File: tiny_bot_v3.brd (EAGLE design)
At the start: 49.7 x 81.5 mm, 31 parts, among them IC1 SN754410PDIP, U1 ATMEGA328P_PDIP, X1 16 MHz

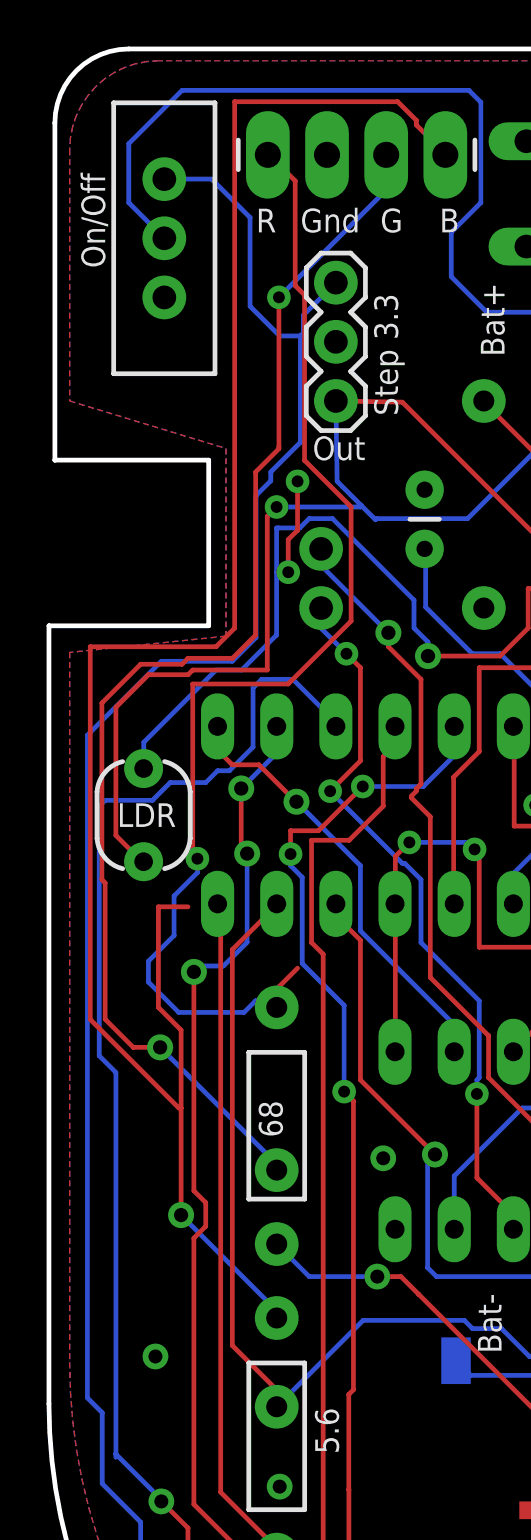
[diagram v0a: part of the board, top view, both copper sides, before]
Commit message: Fixed clearance error and added gerber files
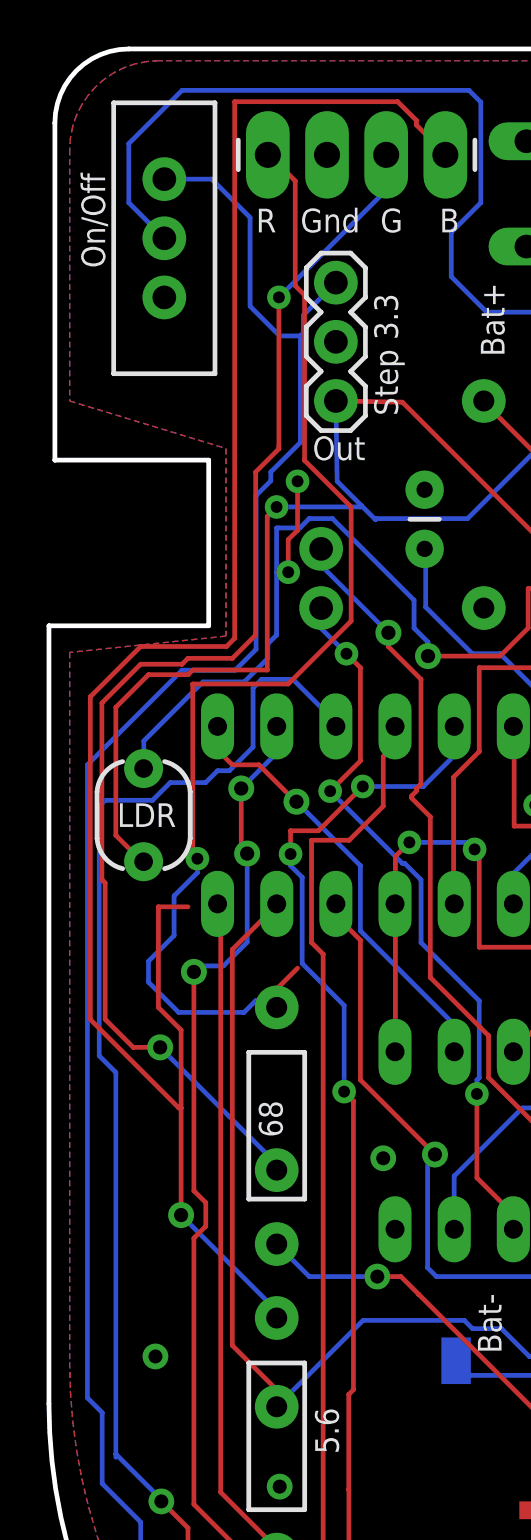
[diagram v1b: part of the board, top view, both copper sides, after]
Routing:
- net N$6: track 81.8 -> 80.7 mm
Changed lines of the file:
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@@
 <wire x1="16.4" y1="54.2" x2="19.5" y2="54.2" width="0.2032" layer="1"/>
 <wire x1="16.4" y1="54.7" x2="16.4" y2="54.2" width="0.2032" layer="16"/>
-<wire x1="4.2" y1="50.5" x2="4.2" y2="49.4" width="0.2032" layer="16"/>
-<wire x1="7.3" y1="53.6" x2="4.2" y2="50.5" width="0.2032" layer="16"/>
-<wire x1="8.4" y1="53.6" x2="7.3" y2="53.6" width="0.2032" layer="16"/>
-<wire x1="9.9" y1="55.1" x2="8.4" y2="53.6" width="0.2032" layer="16"/>
+<wire x1="4.2" y1="50.555" x2="4.2" y2="49.4" width="0.2032" layer="16"/>
 <wire x1="9.9" y1="59.7" x2="9.9" y2="57.800003125" width="0.2032" layer="16"/>
 <wire x1="9.9" y1="57.800003125" x2="9.9" y2="55.1" width="0.2032" layer="16"/>
@@
 <wire x1="36.322" y1="62.865" x2="42.3418" y2="62.865" width="0.2032" layer="16"/>
 <wire x1="42.3418" y1="62.865" x2="45.2374" y2="65.7606" width="0.2032" layer="16"/>
+<wire x1="4.2" y1="50.555" x2="6.731" y2="53.086" width="0.2032" layer="16"/>
+<wire x1="6.731" y1="53.086" x2="8.509" y2="53.086" width="0.2032" layer="16"/>
+<wire x1="8.509" y1="53.086" x2="9.525" y2="54.102" width="0.2032" layer="16"/>
+<wire x1="9.525" y1="54.102" x2="9.525" y2="54.725" width="0.2032" layer="16"/>
+<wire x1="9.525" y1="54.725" x2="9.9" y2="55.1" width="0.2032" layer="16"/>
 </signal>
 <signal name="CENTER_LDR">
@@
 <wire x1="9.652" y1="62.103" x2="9.652" y2="61.722" width="0.2032" layer="16"/>
 <wire x1="9.652" y1="61.722" x2="9.017" y2="61.087" width="0.2032" layer="16"/>
-<wire x1="9.017" y1="61.087" x2="9.017" y2="54.991" width="0.2032" layer="16"/>
-<wire x1="9.017" y1="54.991" x2="8.001" y2="53.975" width="0.2032" layer="16"/>
-<wire x1="8.001" y1="53.975" x2="4.953" y2="53.975" width="0.2032" layer="16"/>
-<wire x1="4.953" y1="53.975" x2="1.778" y2="50.8" width="0.2032" layer="16"/>
-<wire x1="1.778" y1="50.8" x2="1.778" y2="22.352" width="0.2032" layer="16"/>
+<wire x1="9.017" y1="61.087" x2="9.017" y2="54.483" width="0.2032" layer="16"/>
+<wire x1="1.778" y1="49.53" x2="1.778" y2="22.352" width="0.2032" layer="16"/>
+<wire x1="9.017" y1="54.483" x2="8.128" y2="53.594" width="0.2032" layer="16"/>
+<wire x1="8.128" y1="53.594" x2="5.842" y2="53.594" width="0.2032" layer="16"/>
+<wire x1="5.842" y1="53.594" x2="1.778" y2="49.53" width="0.2032" layer="16"/>
 </signal>
 <signal name="N$3">
@@
 <wire x1="15.099996875" y1="78.000003125" x2="15.899996875" y2="77.200003125" width="0.2032" layer="1"/>
 <wire x1="8.099996875" y1="78.000003125" x2="15.099996875" y2="78.000003125" width="0.2032" layer="1"/>
-<wire x1="8.099996875" y1="55.400003125" x2="8.099996875" y2="78.000003125" width="0.2032" layer="1"/>
-<wire x1="7.299996875" y1="54.600003125" x2="8.099996875" y2="55.400003125" width="0.2032" layer="1"/>
-<wire x1="1.899996875" y1="54.600003125" x2="7.299996875" y2="54.600003125" width="0.2032" layer="1"/>
-<wire x1="1.899996875" y1="38.600003125" x2="1.899996875" y2="54.600003125" width="0.2032" layer="1"/>
+<wire x1="8.099996875" y1="54.962996875" x2="8.099996875" y2="78.000003125" width="0.2032" layer="1"/>
 <wire x1="5.699996875" y1="34.800003125" x2="1.899996875" y2="38.600003125" width="0.2032" layer="1"/>
 <wire x1="17.099996875" y1="75.800003125" x2="17.145" y2="75.7174" width="0.2032" layer="1"/>
 <wire x1="5.699996875" y1="34.800003125" x2="5.8" y2="34.800003125" width="0.2032" layer="1"/>
+<wire x1="8.099996875" y1="54.962996875" x2="7.747" y2="54.61" width="0.2032" layer="1"/>
+<wire x1="7.747" y1="54.61" x2="4.064" y2="54.61" width="0.2032" layer="1"/>
+<wire x1="4.064" y1="54.61" x2="1.905" y2="52.451" width="0.2032" layer="1"/>
+<wire x1="1.905" y1="52.451" x2="1.905" y2="38.60500625" width="0.2032" layer="1"/>
+<wire x1="1.905" y1="38.60500625" x2="1.899996875" y2="38.600003125" width="0.2032" layer="1"/>
 </signal>
 <signal name="N$7">
